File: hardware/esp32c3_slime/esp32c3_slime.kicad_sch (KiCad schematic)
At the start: 55 parts, among them J1 USB4105-GF-A, Q1 DMG3415U, SW1 SW_Push, SW2 SW_Push, U1 SHTC3, U2 ICM-42670-P, U3 ESP32-C3-MINI-1, U4 Rust_Board, U5 SY8088, Y1 32.768Hz

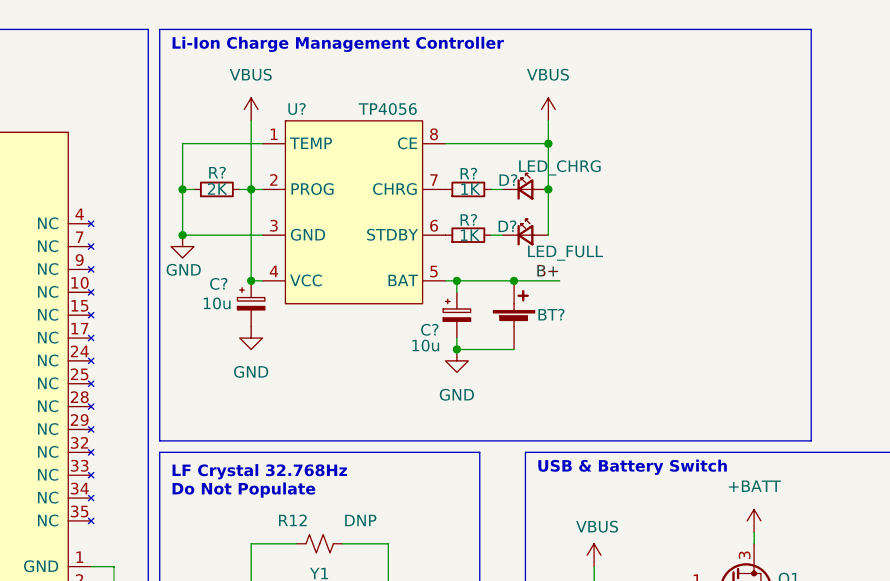
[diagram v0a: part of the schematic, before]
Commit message: Switched charger to TP4056
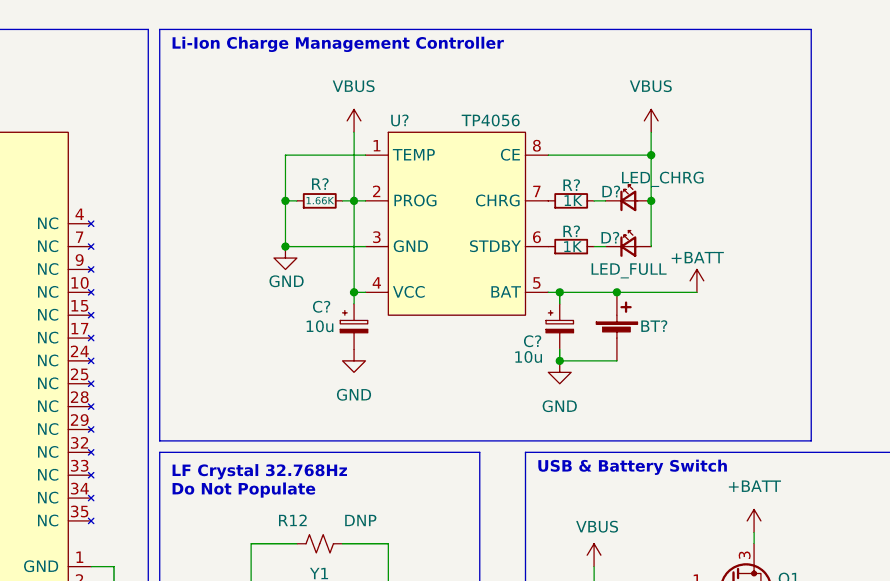
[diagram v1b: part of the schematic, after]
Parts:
- R?: value 2K -> 1.66K
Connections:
- net B+ is gone; now on net +BATT: BT?.1 (+), C?.1, U?.5 (BAT)
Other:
- moved on the sheet: BT?, C?, D?, R?, U?

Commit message: Switched power system to M3406
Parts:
- removed C5, C7: 10uF 16V, Capacitor_SMD:C_0805_2012Metric, symbol Device:C_Small
- removed C6: 22pF 50V, Capacitor_SMD:C_0603_1608Metric, symbol Device:C_Small
- removed L1: SPH4018H2R2MT (2.2uH 2.2A), Inductor_SMD:L_Bourns-SRN4018, symbol Device:L_Small
- removed R1: 10kR, Resistor_SMD:R_0402_1005Metric, symbol Device:R_Small_US
- removed R2: 100kR 1%, Resistor_SMD:R_0402_1005Metric, symbol Device:R_Small_US
- removed R3: 22k1R 1%, Resistor_SMD:R_0402_1005Metric, symbol Device:R_Small_US
- removed U5: SY8088, Package_TO_SOT_SMD:SOT-23-5, symbol Rust_Board:SY8088
- added C? (x2): 470nF, symbol Device:C_Small
- added C?: 10uF, symbol Device:C_Small
- added C?: 4.7uF, symbol Device:C_Small
- added L?: 2.2uH, symbol Device:L
- added R?: 15K, symbol Device:R_Small
- added R?: 68K, symbol Device:R_Small
- added TP?: 3v3, symbol Connector:TestPoint
- added U?: M3406, Package_TO_SOT_SMD:SOT-23-5, symbol slimevr_pcb:M3406
- C? (x2): symbol Device:C_Polarized_Small -> Device:C_Small
- R10, R15, R17, R18, R19, R4, R6, R7, R8: symbol Device:R_Small_US -> Device:R_Small
- R12: symbol Device:R_Small_US -> Device:R_Small; now in the parts list
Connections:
- net +3V3: now also C?.1, C?.1, L?.2, R?.1, TP?.1
- net +5V: now also C?.1, U?.1 (RUN), U?.4 (VIN)
- net GND: now also C?.2, C?.2, C?.2, C?.2, R?.2, U?.2 (GND); no longer J1.S1 (SHELL_GND), J1.S2 (SHELL_GND), J1.S3 (SHELL_GND), J1.S4 (SHELL_GND)
- new net: C?.1, J1.S1 (SHELL_GND), J1.S2 (SHELL_GND), J1.S3 (SHELL_GND), J1.S4 (SHELL_GND)
- new net: R?.1, R?.2, U?.5 (FB)
- new net: L?.1, U?.3 (SW)
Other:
- note added: "Drain"
- note added: "Load"
- note added: "Source"
